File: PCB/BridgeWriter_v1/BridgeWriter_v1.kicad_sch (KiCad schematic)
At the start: 196 parts, among them J1 USB_B, J17 Conn_01x01, J18 Conn_01x01, J2 RJ45_Bel_SI-60062-F, J24 Conn_01x04, J25 Conn_01x04, J3 Conn_01x05, J4 Conn_01x06, J5 Conn_01x02, J6 Conn_01x04, J7 Conn_01x04, J8 Conn_01x02, J9 Micro_SD_Card_Det2, SW1 SW_Push, SW10 SW_Push, SW2 BOOT_MODE0, SW3 SW_Push, SW4 SW_Push, SW5 SW_Push, SW6 SW_Push, SW7 SW_Push, SW8 BOOT_MODE1, SW9 SW_Push, U1 STM32H723VGTx, U10 ADP3338AKCZ-3.3, U11 OKL-T/6-W12N-C, U12 PT86-091940LMR, U13 AM8068, U14 AM8068, U15 MCP9700x-ETT, U16 MCP9700x-ETT, U18 USB_Type-C, U2 W6300, U3 ESP32-C5-WROOM-1, U4 TLP293, U5 MCP2562-E-SN, U6 MCP2562-E-SN, U7 USB3343, U8 ADP3338AKCZ-3.3, U9 CH213K, Y1 FC2012SN 32.768K-70NNA0KC0, Y2 XRCGB25M000FFS1AR0, Y3 ECS-600-8-36B-CTN-TR

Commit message: DFUのType-C追加　FDCANのピン間違い修正　電源供給はUSB PDにしようかなと
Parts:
- added C1: 0.01uF, Capacitor_SMD:C_0603_1608Metric_Pad1.08x0.95mm_HandSolder, symbol Device:C
- added C69: 0.1uF, Capacitor_SMD:C_0603_1608Metric_Pad1.08x0.95mm_HandSolder, symbol Device:C
- added D35: LED, LED_SMD:LED_0603_1608Metric_Pad1.05x0.95mm_HandSolder, symbol Device:LED
- added D4, D7: ESD, Diode_SMD:D_0603_1608Metric_Pad1.05x0.95mm_HandSolder, symbol Device:D_TVS
- added FB2: 600Ω/500mA, Inductor_SMD:L_1206_3216Metric_Pad1.22x1.90mm_HandSolder, symbol Device:FerriteBead
- added R77, R78: 4.7kΩ, Resistor_SMD:R_0402_1005Metric_Pad0.72x0.64mm_HandSolder, symbol Device:R
- added R79: 1kΩ, Resistor_SMD:R_0402_1005Metric_Pad0.72x0.64mm_HandSolder, symbol Device:R
- added U19: CH213K, Package_TO_SOT_SMD:SOT-23, symbol 0_ikeda_symbols:CH213K
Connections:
- net +5V: now also C69.1, U19.2 (VOUT)
- net BOOTMODE: no longer U1.44 (PE14)
- net DEBUG_LED: no longer U1.82 (PD1)
- net ERROR_LED: no longer U1.81 (PD0)
- net Ethernet_RESET: no longer U1.55 (PD8)
- net Ethernet_RX: no longer U1.63 (PC6)
- net Ethernet_TX: no longer U1.62 (PD15)
- net FAN_INA_STM: no longer U1.68 (PA9)
- net FAN_INB_STM: no longer U1.67 (PA8)
- net FDCAN1_RESET: no longer U1.57 (PD10)
- net FDCAN1_RX: no longer U1.98 (PE1)
- net FDCAN1_TX: no longer U1.5 (PE6)
- net FDCAN2_RESET: no longer U1.56 (PD9)
- net FDCAN2_RX: no longer U1.1 (PE2)
- net FDCAN2_TX: no longer U1.4 (PE5)
- net FW_UART_RX: no longer U1.86 (PD5)
- net FW_UART_RXF: no longer U1.88 (PD7)
- net FW_UART_TX: no longer U1.87 (PD6)
- net FW_UART_TXF: no longer U1.92 (PB6)
- net GND: now also U18.A1 (GND), U18.B1 (GND), C1.2, C69.2, D35.1 (K), D4.1 (A1), D7.1 (A1), R77.2, R78.2, U19.1 (GND)
- net PGOOD: no longer U1.69 (PA10)
- net POWER_MONITOR: no longer U1.64 (PC7)
- net SDMMC_CHECK: no longer U1.24 (PA2)
- net SDMMC_READ: no longer U1.22 (PA0)
- net SDMMC_WRITE: no longer U1.23 (PA1)
- net Speaker_In1: no longer U1.3 (PE4)
- net Speaker_In2: no longer U1.2 (PE3)
- net Th_STM: no longer U1.16 (PC1)
- net USB3343_RESETB: no longer U1.45 (PE15)
- net USB_DFU_DM: now also U18.A7 (D-), U18.B7 (D-), D4.2 (A2)
- net USB_DFU_DP: now also U18.A6 (D+), U18.B6 (D+), D7.2 (A2)
- net USB_RESET: no longer U1.54 (PB15)
- net USB_RX: no longer U1.61 (PD14)
- net USB_TX: no longer U1.58 (PD11)
- net W6300_ACT: no longer U1.32 (PC4)
- net W6300_COL: no longer U1.33 (PC5)
- net W6300_DPX: no longer U1.31 (PA7)
- net W6300_INT: no longer U1.42 (PE12)
- net W6300_LNK: no longer U1.28 (PA4)
- net W6300_RST: no longer U1.43 (PE13)
- net W6300_SPD: no longer U1.30 (PA6)
- net WRITER_MODE: no longer U1.84 (PD3)
- net Wi-Fi_RESET: no longer U1.53 (PB14)
- net at U18.A4 (VBUS), U18.B4 (VBUS): now also C1.1, FB2.1, R79.1
- net at U18.A5 (CC1): now also R78.1
- net at U18.B5 (CC2): now also R77.1
- new net: D35.2 (A), R79.2
- new net: FB2.2, U19.3 (VIN)
- no-connect marks 21 -> 24
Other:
- note added: "DFU書き込み完了後はUSB PD給電用として使いたい"
- note added: "STM-DFU"
- note added: "ねじ端子廃止->USB PD給電 DFUのType-Cから給電したい"
- note added: "ファン"
- note added: "ブザー"
- note added: "温度センサー"
- note added: "電源最大入力14V 5VDCDC 3.3Vリニア電源"
- note removed: "USB イーサーネット 無線"
- note removed: "電源最大14V 5VDCDC 3.3Vリニア電源"
- moved on the sheet: C10, C11, C12, C13, C14, C15, C16, C17, C18, C19, C2, C20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
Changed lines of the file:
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@@
 	(generator "eeschema")
 	(generator_version "9.0")
-	(paper "A2")
+	(paper "A1")

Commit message: 基板にTVSダイオードと逆接保護追加　給電をUSB PD かDC ジャックにしようと思う　サージ電圧保護とOCPとOVPを追加する予定
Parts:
- removed J17, J18: Conn_01x01, 0Ikedalibrary:5x5, symbol Connector_Generic:Conn_01x01
- removed U10, U8: ADP3338AKCZ-3.3, Package_TO_SOT_SMD:SOT-223-3_TabPin2, symbol My_Library:ADP3338AKCZ-3.3
- added D13: SS2040FL, My_Library:SS2040FL, symbol Device:D_Filled
- added D8: SB34AFC, My_Library:SB34AFC, symbol My_Library:SB34AFC
- added D9: ESD, Diode_SMD:D_0603_1608Metric_Pad1.05x0.95mm_HandSolder, symbol Device:D_TVS
- added J10: Barrel_Jack_MountingPin, My_Library:DC_Jack_18742, symbol Connector:Barrel_Jack_MountingPin
- added R16: 1mΩ, Resistor_SMD:R_2512_6332Metric_Pad1.40x3.35mm_HandSolder, symbol Device:R
- added R28, R29: 100, Resistor_SMD:R_0603_1608Metric_Pad0.98x0.95mm_HandSolder, symbol Device:R_Small
- added R48, R49: 100k, Resistor_SMD:R_0603_1608Metric_Pad0.98x0.95mm_HandSolder, symbol Device:R_Small
- added U10, U8: TPS1117LV33S, Package_TO_SOT_SMD:SOT-223-3_TabPin2, symbol My_Library:TPS1117LV33S
- added U20: KIA75S358F, Package_TO_SOT_SMD:SOT-23-5, symbol My_Library:KIA75S358F
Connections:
- net +3.3V: now also U20.5 (Vcc), U8.2 (Vout)
- net +5V: now also D8.2 (A), U10.3 (Vin), U8.3 (Vin); no longer J24.3 (Pin_3), J25.3 (Pin_3), J6.3 (Pin_3), J7.3 (Pin_3)
- net ESP_3.3V: now also U10.2 (Vout)
- net Ethernet_RESET: now also R20.2
- net FDCAN1_RESET: now also R21.2
- net FDCAN2_RESET: now also R22.2
- net GND: now also SW3.1, SW4.1, SW5.1, SW6.1, SW7.1, D13.2 (A), D9.1 (A1), J10.2, R49.2, U10.1 (GND), U20.2 (Gnd), U8.1 (GND)
- net USB_RESET: now also R19.2
- net VCC: now also D13.1 (K), D9.2 (A2), J10.1, R16.1, R28.1; no longer C37.1, U11.2 (Vin)
- net Wi-Fi_RESET: now also R61.2
- new net: R29.2, R49.1, U20.1 (+)
- new net: R48.1, U20.4
- new net: R28.2, R48.2, U20.3 (-)
- new net +5VA: D8.1 (K), J24.3 (Pin_3), J25.3 (Pin_3), J6.3 (Pin_3), J7.3 (Pin_3)
- new net VCC_IO: C37.1, R16.2, R29.1, U11.2 (Vin)
- no-connect marks 24 -> 25
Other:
- note added: "ねじ端子廃止->USB PD給電 かDCジャックから DFUのType-Cから給電したい"
- note added: "通信リセット"
- note removed: "ねじ端子廃止->USB PD給電 DFUのType-Cから給電したい"
- moved on the sheet: C1, C25, C26, C44, C66, C67, C68, C69, D35, D4, D7, FB2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

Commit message: USB PD追加
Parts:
- removed C29: 1uF, Capacitor_SMD:C_0603_1608Metric_Pad1.08x0.95mm_HandSolder, symbol Device:C_Small
- removed C69: 0.1uF, Capacitor_SMD:C_0603_1608Metric_Pad1.08x0.95mm_HandSolder, symbol Device:C
- removed D48: ESD, Diode_SMD:D_0603_1608Metric_Pad1.05x0.95mm_HandSolder, symbol Device:D_TVS
- removed FB1: 600Ω/500mA, Inductor_SMD:L_0603_1608Metric_Pad1.05x0.95mm_HandSolder, symbol Device:FerriteBead_Small
- removed FB2: 600Ω/500mA, Inductor_SMD:L_1206_3216Metric_Pad1.22x1.90mm_HandSolder, symbol Device:FerriteBead
- removed U19, U9: CH213K, Package_TO_SOT_SMD:SOT-23, symbol 0_ikeda_symbols:CH213K
- added D11, D12: SS2040FL, My_Library:SS2040FL, symbol Device:D_Filled
- added J11: USB_C_Receptacle_PowerOnly_6P, My_Library:632722100213, symbol Connector:USB_C_Receptacle_PowerOnly_6P
- added R52: 10k, Resistor_SMD:R_0603_1608Metric_Pad0.98x0.95mm_HandSolder, symbol Device:R_Small
- added R65: 1k, Resistor_SMD:R_0603_1608Metric_Pad0.98x0.95mm_HandSolder, symbol Device:R_Small
- added R66: 24k, Resistor_SMD:R_0603_1608Metric_Pad0.98x0.95mm_HandSolder, symbol Device:R_Small
- added U21: TLP293, Package_SO:SOIC-4_4.55x2.6mm_P1.27mm, symbol Isolator:TLP293
- added U9: CH221K, Package_TO_SOT_SMD:SOT-23-6_Handsoldering, symbol My_Library:CH221K
- C7: value 0.1uF -> 1uF; footprint Capacitor_SMD:C_0603_1608Metric_Pad1.08x0.95mm_HandSolder -> Capacitor_SMD:C_0402_1005Metric_Pad0.74x0.62mm_HandSolder
- R48, R49: value 100k -> 50k
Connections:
- net +3.3V: now also R65.2
- net +5V: now also D11.2 (A); no longer C7.1
- net GND: now also J11.A12 (GND), J11.B12 (GND), R66.2, U21.2, U9.2 (GND)
- net VBUS: now also C1.1, C7.1, R79.1, U18.A4 (VBUS), U18.B4 (VBUS), D11.1 (K), D12.1 (K), U9.1 (VDD); no longer J1.1 (VBUS)
- net VCC: now also J11.A9 (VBUS), J11.B9 (VBUS)
- net POWER_ADC: now reaches R28.2, R48.2, U20.3 (-)
- new net: J11.A5 (CC1), U9.4 (CC1)
- new net: J11.B5 (CC2), U9.5 (CC2)
- new net: R66.1, U9.6 (CFG)
- new net: D12.2 (A), J1.1 (VBUS), R52.1
- new net: R65.1, U21.4
- new net: R52.2, U21.1
- new net USB_HS_CHECK: U21.3
- new net USB_PD_GOOD: U9.3 (PG)
- no-connect marks 25 -> 26
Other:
- note removed: "DFU書き込み完了後はUSB PD給電用として使いたい"

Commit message: フォルダの作成
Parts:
- removed D11, D12: SS2040FL, My_Library:SS2040FL, symbol Device:D_Filled
- added C29, C69, C70: 0.1uF, Capacitor_SMD:C_0603_1608Metric_Pad1.08x0.95mm_HandSolder, symbol Device:C
- added FB1, FB2: 600Ω/500mA, Inductor_SMD:L_1206_3216Metric_Pad1.22x1.90mm_HandSolder, symbol Device:FerriteBead
- added U19, U22, U23: CH213K, Package_TO_SOT_SMD:SOT-23, symbol 0_ikeda_symbols:CH213K
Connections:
- net +5V: now also U23.3 (VIN)
- net GND: now also C29.2, C69.2, C70.2, U19.1 (GND), U22.1 (GND), U23.1 (GND)
- net VBUS: now also C29.1, C69.1, C70.1, U19.2 (VOUT), U22.2 (VOUT), U23.2 (VOUT); no longer C1.1, R79.1, U18.A4 (VBUS), U18.B4 (VBUS)
- net at J1.1 (VBUS), R52.1: now also FB2.1
- new net: C1.1, FB1.1, R79.1, U18.A4 (VBUS), U18.B4 (VBUS)
- new net: FB2.2, U22.3 (VIN)
- new net: FB1.2, U19.3 (VIN)
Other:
- note added: "3.3 リニア"
- note added: "5V DCDC"
- note added: "Bridge-Writer_v1"
- note added: "DCジャック"
- note added: "FDCAN1"
- note added: "FDCAN2"
- note added: "HSE"
- note added: "LSE"
- note added: "MCU RESET"
- note added: "USB PD"
- note added: "USB_OTG_HS_ULPI"
- note added: "外部クロック"
- note added: "消費電流監視"
- note added: "起動モード"
- note added: "逆流保護"
- note added: "電源断用一時電源"
- note added: "電源確認"
- note removed: "Bridge-Writer_v0"
- note removed: "USB_OTH_HS_ULPI"
- moved on the sheet: C10, C3, C30, C31, C32, C33, C34, C36, C37, C38, C39, C4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

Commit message: docs : PCB作成途中　書き込み基板のPCBを一から作り直し
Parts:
- added C71: 0.1uF, Capacitor_SMD:C_0402_1005Metric_Pad0.74x0.62mm_HandSolder, symbol Device:C_Small
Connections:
- net +3.3V: now also C71.1
- net FDCAN1_RESET: now also SW3.2; no longer SW4.2
- net FDCAN2_RESET: now also SW4.2; no longer SW3.2
- net GND: now also C71.2
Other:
- moved on the sheet: SW3, SW4

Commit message: PCB電源LED以外配線終わり　やること　LED追加と、シルクの被り解消
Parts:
- added C72, C73: 0.1uF, Capacitor_SMD:C_0402_1005Metric_Pad0.74x0.62mm_HandSolder, symbol Device:C_Small
- added J12, J13: Conn_01x01, 0Ikedalibrary:5x5, symbol Connector_Generic:Conn_01x01
- C25, C26, C66, C67, C68: footprint Capacitor_SMD:C_0603_1608Metric_Pad1.08x0.95mm_HandSolder -> Capacitor_SMD:C_0402_1005Metric_Pad0.74x0.62mm_HandSolder
- FB1, FB2: footprint Inductor_SMD:L_1206_3216Metric_Pad1.22x1.90mm_HandSolder -> Inductor_SMD:L_0603_1608Metric_Pad1.05x0.95mm_HandSolder
- R19, R20, R21, R22, R53, R61: footprint Resistor_SMD:R_0603_1608Metric_Pad0.98x0.95mm_HandSolder -> Resistor_SMD:R_0402_1005Metric_Pad0.72x0.64mm_HandSolder
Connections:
- net +3.3V: now also U16.1 (V_{DD}), C72.1
- net +5V: no longer U15.1 (V_{DD}), U16.1 (V_{DD})
- net BOOTMODE: now also U1.64 (PC7)
- net DEBUG_LED: now also U1.2 (PE3)
- net ERROR_LED: now also U1.1 (PE2)
- net ESP_3.3V: now also U15.1 (V_{DD}), C73.1
- net Ethernet_RESET: now also U1.55 (PD8)
- net Ethernet_RX: now also U1.63 (PC6)
- net Ethernet_TX: now also U1.62 (PD15)
- net FAN_INA_STM: now also U1.5 (PE6)
- net FAN_INB_STM: now also U1.4 (PE5)
- net FDCAN1_RESET: now also U1.53 (PB14)
- net FDCAN1_RX: now also U1.85 (PD4)
- net FDCAN1_TX: now also U1.84 (PD3)
- net FDCAN2_RESET: now also U1.54 (PB15)
- net FDCAN2_RX: now also U1.82 (PD1)
- net FDCAN2_TX: now also U1.81 (PD0)
- net GND: now also C72.2, C73.2, J13.1 (Pin_1)
- net PGOOD: now also U1.22 (PA0)
- net POWER_ADC: now also U1.23 (PA1)
- net POWER_MONITOR: now also U1.7 (PC13)
- net SDMMC_CHECK: now also U1.67 (PA8)
- net SDMMC_READ: now also U1.87 (PD6)
- net SDMMC_WRITE: now also U1.86 (PD5)
- net Speaker_In1: now also U1.68 (PA9)
- net Speaker_In2: now also U1.69 (PA10)
- net Th_STM: now also U1.16 (PC1)
- net USB3343_RESETB: now also U1.45 (PE15)
- net USB_HS_CHECK: now also U1.44 (PE14)
- net USB_PD_GOOD: now also U1.24 (PA2)
- net USB_RESET: now also U1.56 (PD9)
- net USB_RX: now also U1.61 (PD14)
- net USB_TX: now also U1.58 (PD11)
- net VBUS: no longer R57.2
- net VCC: now also J12.1 (Pin_1)
- net W6300_ACT: now also U1.32 (PC4)
- net W6300_COL: now also U1.33 (PC5)
- net W6300_DPX: now also U1.31 (PA7)
- net W6300_INT: now also U1.42 (PE12)
- net W6300_LNK: now also U1.28 (PA4)
- net W6300_RST: now also U1.43 (PE13)
- net W6300_SPD: now also U1.30 (PA6)
- net WRITER_MODE: now also U1.3 (PE4)
- net Wi-Fi_RESET: now also U1.57 (PD10)
- net HS_VBUS: now reaches FB2.1, J1.1 (VBUS), R52.1
- net HS_VBUS: now also R57.2
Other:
- note added: "MCP9700T-E/TT"
- note added: "ねじ端子"
- note removed: "MCP9700BT-E/TT"
- note removed: "ねじ端子廃止->USB PD給電 かDCジャックから DFUのType-Cから給電したい"
- moved on the sheet: J8, R45, R64, U14, U15

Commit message: ほぼ完成
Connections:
- net FAN_INA_ESP: now also U3.14 (IO14); no longer U3.18 (IO27)
- net FAN_INB_ESP: now also U3.13 (IO13); no longer U3.15 (IO28)
- net FW_UART_RX: now also U1.87 (PD6), U3.17 (IO4); no longer U3.16 (IO5)
- net FW_UART_RXF: now also U1.98 (PE1), U3.18 (IO27); no longer U3.19 (IO15)
- net FW_UART_TX: now also U1.86 (PD5), U3.16 (IO5); no longer U3.17 (IO4)
- net FW_UART_TXF: now also U1.97 (PE0), U3.15 (IO28); no longer U3.21 (IO23)
- net SDMMC_READ: now also U1.93 (PB7); no longer U1.87 (PD6)
- net SDMMC_WRITE: now also U1.92 (PB6); no longer U1.86 (PD5)
- net Wi-Fi_RX: now also U3.19 (IO15); no longer U3.13 (IO13)
- net Wi-Fi_TX: now also U3.21 (IO23); no longer U3.14 (IO14)

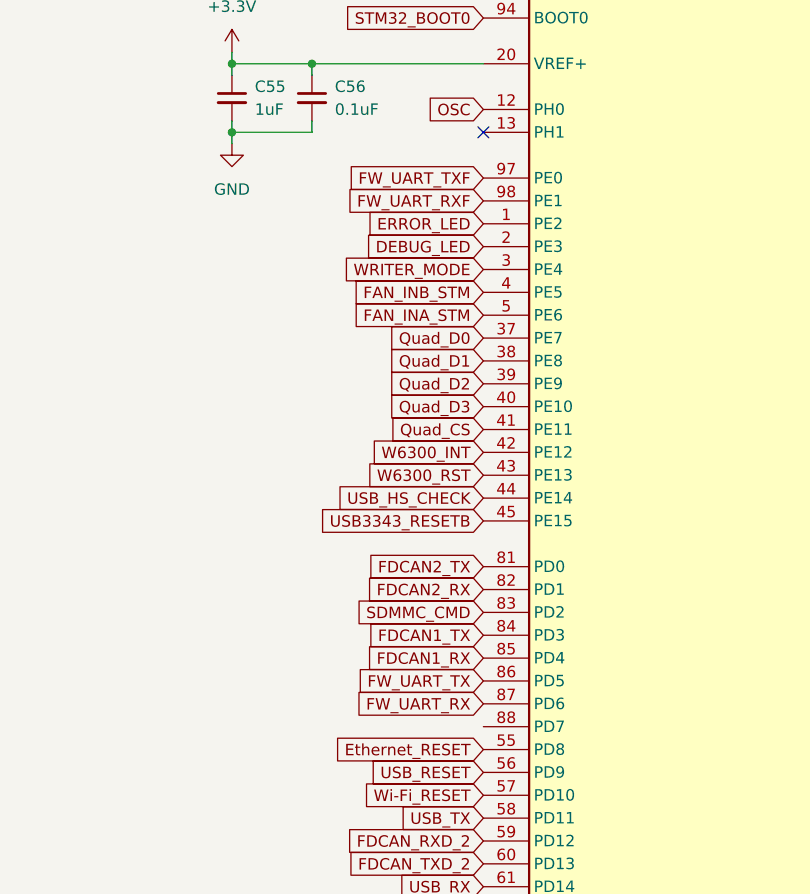
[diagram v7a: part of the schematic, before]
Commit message: feat : GENERATE CODE fdcanクラスの作成
ブランチの追加たがまだわかっていないので次回からブランチを使います。
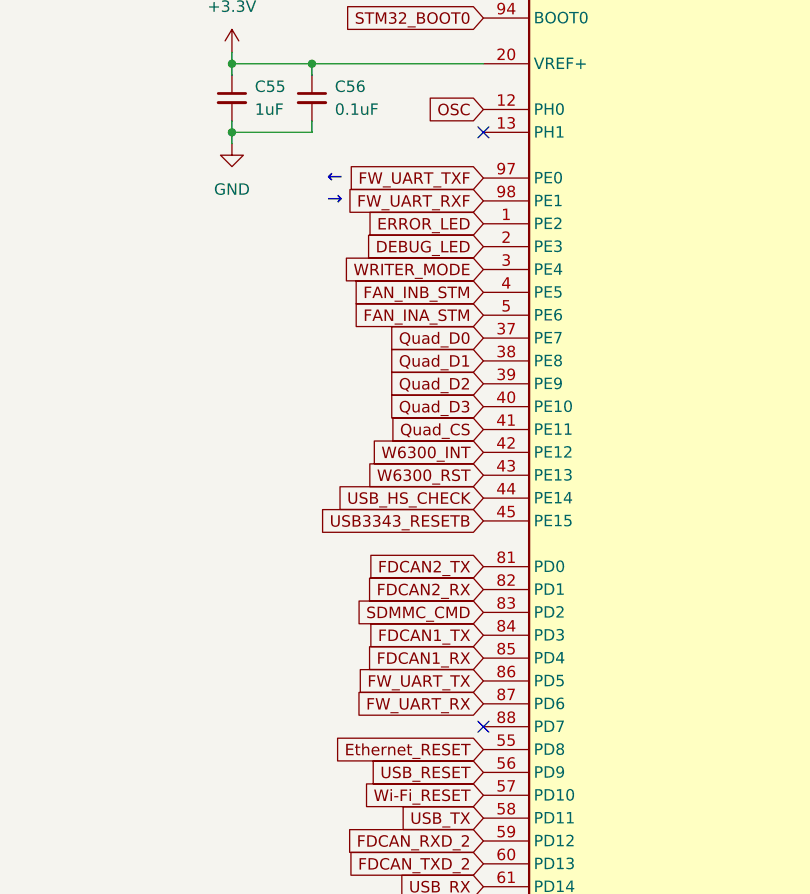
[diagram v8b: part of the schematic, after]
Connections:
- no-connect marks 26 -> 27
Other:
- note added: "← →"
